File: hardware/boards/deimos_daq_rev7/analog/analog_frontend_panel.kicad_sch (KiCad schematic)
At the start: 18 parts, among them IC3001 BD42540FJ-CE2, IC3002 BD42540FJ-CE2, IC3003 BD42540FJ-CE2, J3001 Screw_Terminal_01x12, J3002 Screw_Terminal_01x10, J3003 Screw_Terminal_01x12, J3004 Screw_Terminal_01x12, J3005 Screw_Terminal_01x10, J3006 Screw_Terminal_01x12

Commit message: replace user power with gpio. wip to update frontend layout.
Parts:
- removed C3001, C3002: 0.1uF 50V 0603, Capacitor_SMD:C_0603_1608Metric, symbol Device:C_Small
- removed IC3001, IC3003: BD42540FJ-CE2, aaa:SOIC127P600X175-8N, symbol aaa:BD42540FJ-CE2
- removed J3001, J3003, J3004, J3006: Screw_Terminal_01x12, aaa:KF141V-2.54-12P, symbol Connector:Screw_Terminal_01x12
- removed J3002, J3005: Screw_Terminal_01x10, aaa:KF141V-2.54-10P, symbol Connector:Screw_Terminal_01x10
- added J1001, J1002, J1003, J1004, J1005, J1007: WJ15EDGRM-3.81-12P, aaa:WJ15EDGRM-3.81-12P, symbol aaa:WJ15EDGRM-3.81-12P
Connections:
- net 4-20mA Frontend/+24_EXC: now also J1004.11
- net 4-20mA Frontend/SIGNAL: now also J1004.12
- net 4-20mA Frontend1/+24_EXC: now also J1004.8
- net 4-20mA Frontend1/SIGNAL: now also J1004.9
- net 4-20mA Frontend2/+24_EXC: now also J1004.5
- net 4-20mA Frontend2/SIGNAL: now also J1004.6
- net 4-20mA Frontend3/+24_EXC: now also J1004.2
- net 4-20mA Frontend3/SIGNAL: now also J1004.3
- net GND: now also J1001.1, J1001.3, J1001.5, J1001.7, J1001.9, J1002.1, J1002.11, J1002.3, J1002.5, J1002.7, J1002.9, J1003.1, J1003.11, J1003.3, J1003.5, J1003.7, J1003.9, J1004.1, J1004.10, J1004.4, J1004.7, J1007.1, J1007.11, J1007.3, J1007.5, J1007.7, J1007.9
- net RTD Amp/R+: now also J1005.9
- net RTD Amp/R-: now also J1005.8
- net RTD Amp/W-: now also J1005.7
- net RTD Amp1/R+: now also J1005.6
- net RTD Amp1/R-: now also J1005.5
- net RTD Amp1/W-: now also J1005.4
- net RTD Amp2/R+: now also J1005.3
- net RTD Amp2/R-: now also J1005.2
- net RTD Amp2/W-: now also J1005.1
- net ain_0-15V_/VIN: now also J1003.8
- net ain_0-15V_1/VIN: now also J1003.6
- net ain_g1_/VIN: now also J1003.12
- net ain_g1_1/VIN: now also J1003.10
- net ain_g25p7_/VIN: now also J1003.4
- net ain_g666p333_/VIN: now also J1003.2
- net dac_buf/VOUT: now also J1002.2
- net dac_buf1/VOUT: now also J1002.4
- net pwm_in_buf/VIN: now also J1001.4
- net pwm_in_buf1/VIN: now also J1001.2
- net pwm_in_buf2/VIN: now also J1001.10
- net pwm_in_buf3/VIN: now also J1001.8
- net pwm_in_buf4/VIN: now also J1001.6
- net pwm_out_buf/VOUT: now also J1002.6
- net pwm_out_buf1/VOUT: now also J1002.8
- net pwm_out_buf2/VOUT: now also J1002.10
- net pwm_out_buf3/VOUT: now also J1002.12
- new net pwm_in_buf5/VIN: J1007.2
- new net pwm_in_buf6/VIN: J1007.4
- new net pwm_in_buf7/VIN: J1007.6
- new net pwm_out_buf4/VOUT: J1007.8
- new net pwm_out_buf5/VOUT: J1007.10
- new net pwm_out_buf6/VOUT: J1007.12
- no-connect marks 1 -> 5
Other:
- added sheet pwm_in_buf5 (pwm_in_buf.kicad_sch)
- added sheet pwm_in_buf6 (pwm_in_buf.kicad_sch)
- added sheet pwm_in_buf7 (pwm_in_buf.kicad_sch)
- added sheet pwm_out_buf4 (pwm_out_buf.kicad_sch)
- added sheet pwm_out_buf5 (pwm_out_buf.kicad_sch)
- added sheet pwm_out_buf6 (pwm_out_buf.kicad_sch)
- note added: "GPIO w/ OVP"
- note removed: "70mA total"
- note removed: "LDO for short-circuit protection"
- note removed: "User Power"

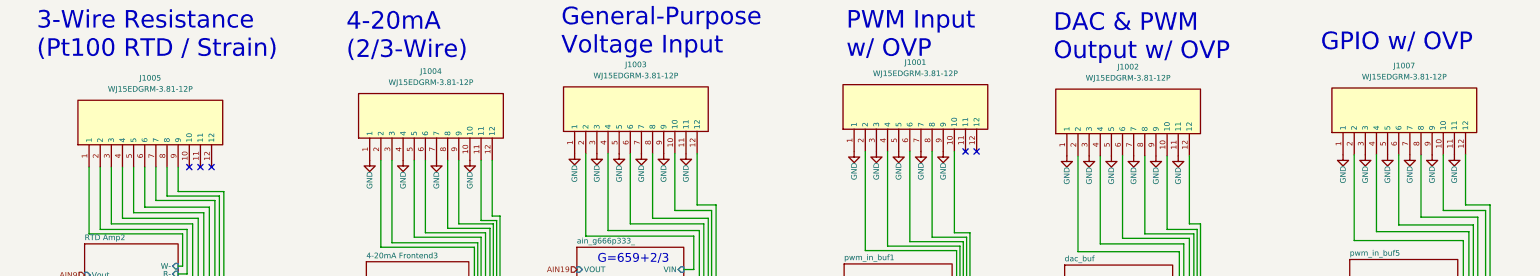
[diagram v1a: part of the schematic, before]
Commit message: flip pin order in symbol for pluggable terminal block
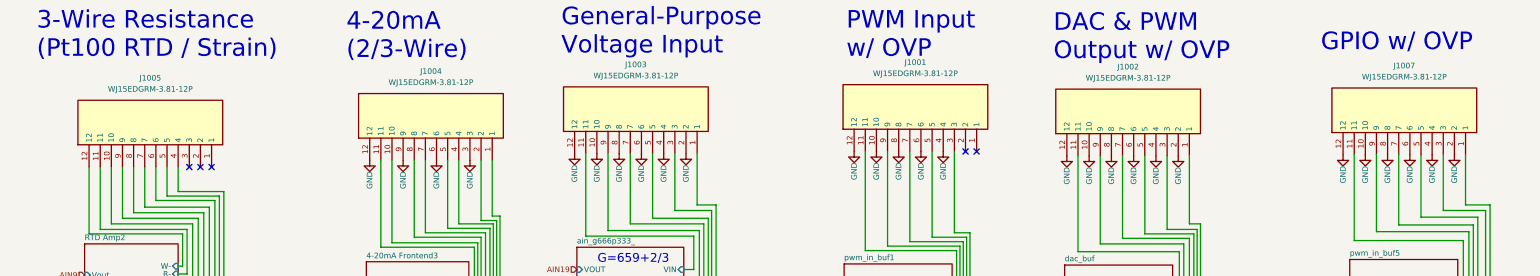
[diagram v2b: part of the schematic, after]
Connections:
- net 4-20mA Frontend/+24_EXC: now also J1004.2; no longer J1004.11
- net 4-20mA Frontend/SIGNAL: now also J1004.1; no longer J1004.12
- net 4-20mA Frontend1/+24_EXC: now also J1004.5; no longer J1004.8
- net 4-20mA Frontend1/SIGNAL: now also J1004.4; no longer J1004.9
- net 4-20mA Frontend2/+24_EXC: now also J1004.8; no longer J1004.5
- net 4-20mA Frontend2/SIGNAL: now also J1004.7; no longer J1004.6
- net 4-20mA Frontend3/+24_EXC: now also J1004.11; no longer J1004.2
- net 4-20mA Frontend3/SIGNAL: now also J1004.10; no longer J1004.3
- net GND: now also J1001.10, J1001.12, J1001.4, J1001.6, J1001.8, J1002.10, J1002.12, J1002.2, J1002.4, J1002.6, J1002.8, J1003.10, J1003.12, J1003.2, J1003.4, J1003.6, J1003.8, J1004.12, J1004.3, J1004.6, J1004.9, J1007.10, J1007.12, J1007.2, J1007.4, J1007.6, J1007.8; no longer J1001.1, J1001.3, J1001.5, J1001.7, J1001.9, J1002.1, J1002.11, J1002.3, J1002.5, J1002.7, J1002.9, J1003.1, J1003.11, J1003.3, J1003.5, J1003.7, J1003.9, J1004.1, J1004.10, J1004.4, J1004.7, J1007.1, J1007.11, J1007.3, J1007.5, J1007.7, J1007.9
- net RTD Amp/R+: now also J1005.4; no longer J1005.9
- net RTD Amp/R-: now also J1005.5; no longer J1005.8
- net RTD Amp/W-: now also J1005.6; no longer J1005.7
- net RTD Amp1/R+: now also J1005.7; no longer J1005.6
- net RTD Amp1/R-: now also J1005.8; no longer J1005.5
- net RTD Amp1/W-: now also J1005.9; no longer J1005.4
- net RTD Amp2/R+: now also J1005.10; no longer J1005.3
- net RTD Amp2/R-: now also J1005.11; no longer J1005.2
- net RTD Amp2/W-: now also J1005.12; no longer J1005.1
- net ain_0-15V_/VIN: now also J1003.5; no longer J1003.8
- net ain_0-15V_1/VIN: now also J1003.7; no longer J1003.6
- net ain_g1_/VIN: now also J1003.1; no longer J1003.12
- net ain_g1_1/VIN: now also J1003.3; no longer J1003.10
- net ain_g25p7_/VIN: now also J1003.9; no longer J1003.4
- net ain_g666p333_/VIN: now also J1003.11; no longer J1003.2
- net dac_buf/VOUT: now also J1002.11; no longer J1002.2
- net dac_buf1/VOUT: now also J1002.9; no longer J1002.4
- net pwm_in_buf/VIN: now also J1001.9; no longer J1001.4
- net pwm_in_buf1/VIN: now also J1001.11; no longer J1001.2
- net pwm_in_buf2/VIN: now also J1001.3; no longer J1001.10
- net pwm_in_buf3/VIN: now also J1001.5; no longer J1001.8
- net pwm_in_buf4/VIN: now also J1001.7; no longer J1001.6
- net pwm_in_buf5/VIN: now also J1007.11; no longer J1007.2
- net pwm_in_buf6/VIN: now also J1007.9; no longer J1007.4
- net pwm_in_buf7/VIN: now also J1007.7; no longer J1007.6
- net pwm_out_buf/VOUT: now also J1002.7; no longer J1002.6
- net pwm_out_buf1/VOUT: now also J1002.5; no longer J1002.8
- net pwm_out_buf2/VOUT: now also J1002.3; no longer J1002.10
- net pwm_out_buf3/VOUT: now also J1002.1; no longer J1002.12
- net pwm_out_buf4/VOUT: now also J1007.5; no longer J1007.8
- net pwm_out_buf5/VOUT: now also J1007.3; no longer J1007.10
- net pwm_out_buf6/VOUT: now also J1007.1; no longer J1007.12

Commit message: position connectors
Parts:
- renumbered J1005 to J3001, J1004 to J3002, J1003 to J3003, J1001 to J3004, J1002 to J3005, J1007 to J3006
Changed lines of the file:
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@@
 		(dnp no)
 		(fields_autoplaced yes)
-		(property "Reference" "J1005"
+		(property "Reference" "J3001"
 			(at 147.32 28.448 90)
 			(effects
@@
 		)
 		(instances
+			(project "analog_i"
+				(path "/5a60c4b1-b6cb-416e-8883-8291fa089b87/c2baf18d-2b19-4edb-98b3-535275ee271f"
+					(reference "J3001")
+					(unit 1)
+				)
+			)
 			(project "analog_frontend_panel"
 				(path "/c241d083-1323-4b4a-a540-956d0afb7b72"
@@
 		(dnp no)
 		(fields_autoplaced yes)
-		(property "Reference" "J1007"
+		(property "Reference" "J3006"
 			(at 433.324 25.654 90)
 			(effects
@@
 		)
 		(instances
+			(project "analog_i"
+				(path "/5a60c4b1-b6cb-416e-8883-8291fa089b87/c2baf18d-2b19-4edb-98b3-535275ee271f"
+					(reference "J3006")
+					(unit 1)
+				)
+			)
 			(project "analog_frontend_panel"
 				(path "/c241d083-1323-4b4a-a540-956d0afb7b72"
@@
 		(dnp no)
 		(fields_autoplaced yes)
-		(property "Reference" "J1003"
+		(property "Reference" "J3003"
 			(at 258.064 25.4 90)
 			(effects
@@
 		)
 		(instances
+			(project "analog_i"
+				(path "/5a60c4b1-b6cb-416e-8883-8291fa089b87/c2baf18d-2b19-4edb-98b3-535275ee271f"
+					(reference "J3003")
+					(unit 1)
+				)
+			)
 			(project "analog_frontend_panel"
 				(path "/c241d083-1323-4b4a-a540-956d0afb7b72"
@@
 		(dnp no)
 		(fields_autoplaced yes)
-		(property "Reference" "J1004"
+		(property "Reference" "J3002"
 			(at 211.328 26.924 90)
 			(effects
@@
 		)
 		(instances
+			(project "analog_i"
+				(path "/5a60c4b1-b6cb-416e-8883-8291fa089b87/c2baf18d-2b19-4edb-98b3-535275ee271f"
+					(reference "J3002")
+					(unit 1)
+				)
+			)
 			(project "analog_frontend_panel"
 				(path "/c241d083-1323-4b4a-a540-956d0afb7b72"
@@
 		(on_board yes)
 		(dnp no)
-		(property "Reference" "#PWR1028"
+		(property "Reference" "#PWR106"
 			(at 429.514 52.324 0)
 			(effects
@@
 		)
 		(instances
+			(project "analog_i"
+				(path "/5a60c4b1-b6cb-416e-8883-8291fa089b87/c2baf18d-2b19-4edb-98b3-535275ee271f"
+					(reference "#PWR106")
+					(unit 1)
+				)
+			)
 			(project "analog_frontend_panel"
 				(path "/c241d083-1323-4b4a-a540-956d0afb7b72"
@@
 		(dnp no)
 		(fields_autoplaced yes)
-		(property "Reference" "J1001"
+		(property "Reference" "J3004"
 			(at 321.818 24.892 90)
 			(effects
@@
 		)
 		(instances
+			(project "analog_i"
+				(path "/5a60c4b1-b6cb-416e-8883-8291fa089b87/c2baf18d-2b19-4edb-98b3-535275ee271f"
+					(reference "J3004")
+					(unit 1)
+				)
+			)
 			(project "analog_frontend_panel"
 				(path "/c241d083-1323-4b4a-a540-956d0afb7b72"
@@
 		(dnp no)
 		(fields_autoplaced yes)
-		(property "Reference" "J1002"
+		(property "Reference" "J3005"
 			(at 370.332 25.908 90)
 			(effects
@@
 		)
 		(instances
+			(project "analog_i"
+				(path "/5a60c4b1-b6cb-416e-8883-8291fa089b87/c2baf18d-2b19-4edb-98b3-535275ee271f"
+					(reference "J3005")
+					(unit 1)
+				)
+			)
 			(project ""
 				(path "/c241d083-1323-4b4a-a540-956d0afb7b72"
@@
 		(on_board yes)
 		(dnp no)
-		(property "Reference" "#PWR1029"
+		(property "Reference" "#PWR110"
 			(at 434.594 52.324 0)
 			(effects
@@
 		)
 		(instances
+			(project "analog_i"
+				(path "/5a60c4b1-b6cb-416e-8883-8291fa089b87/c2baf18d-2b19-4edb-98b3-535275ee271f"
+					(reference "#PWR110")
+					(unit 1)
+				)
+			)
 			(project "analog_frontend_panel"
 				(path "/c241d083-1323-4b4a-a540-956d0afb7b72"
@@
 		(on_board yes)
 		(dnp no)
-		(property "Reference" "#PWR1027"
+		(property "Reference" "#PWR109"
 			(at 424.434 52.324 0)
 			(effects
@@
 		)
 		(instances
+			(project "analog_i"
+				(path "/5a60c4b1-b6cb-416e-8883-8291fa089b87/c2baf18d-2b19-4edb-98b3-535275ee271f"
+					(reference "#PWR109")
+					(unit 1)
+				)
+			)
 			(project "analog_frontend_panel"
 				(path "/c241d083-1323-4b4a-a540-956d0afb7b72"
@@
 		(on_board yes)
 		(dnp no)
-		(property "Reference" "#PWR1032"
+		(property "Reference" "#PWR104"
 			(at 444.754 52.324 0)
 			(effects
@@
 		)
 		(instances
+			(project "analog_i"
+				(path "/5a60c4b1-b6cb-416e-8883-8291fa089b87/c2baf18d-2b19-4edb-98b3-535275ee271f"
+					(reference "#PWR104")
+					(unit 1)
+				)
+			)
 			(project "analog_frontend_panel"
 				(path "/c241d083-1323-4b4a-a540-956d0afb7b72"
@@
 		(on_board yes)
 		(dnp no)
-		(property "Reference" "#PWR1031"
+		(property "Reference" "#PWR105"
 			(at 439.674 52.324 0)
 			(effects
@@
 		)
 		(instances
+			(project "analog_i"
+				(path "/5a60c4b1-b6cb-416e-8883-8291fa089b87/c2baf18d-2b19-4edb-98b3-535275ee271f"
+					(reference "#PWR105")
+					(unit 1)
+				)
+			)
 			(project "analog_frontend_panel"
 				(path "/c241d083-1323-4b4a-a540-956d0afb7b72"
@@
 		(on_board yes)
 		(dnp no)
-		(property "Reference" "#PWR1026"
+		(property "Reference" "#PWR111"
 			(at 419.354 52.324 0)
 			(effects
@@
 		)
 		(instances
+			(project "analog_i"
+				(path "/5a60c4b1-b6cb-416e-8883-8291fa089b87/c2baf18d-2b19-4edb-98b3-535275ee271f"
+					(reference "#PWR111")
+					(unit 1)
+				)
+			)
 			(project "analog_frontend_panel"
 				(path "/c241d083-1323-4b4a-a540-956d0afb7b72"

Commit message: wip to update layout for frontend
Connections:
- net pwm_in_buf5/VIN is gone; now on net pwm_in_buf6/VIN: J3006.11
- net pwm_in_buf6/VIN: no longer J3006.9
- net pwm_in_buf7/VIN: now also J3006.9; no longer J3006.7
- net pwm_out_buf4/VOUT: now also J3006.7; no longer J3006.5
- net pwm_out_buf5/VOUT: now also J3006.5; no longer J3006.3
- net pwm_out_buf6/VOUT: now also J3006.3; no longer J3006.1
- new net pwm_out_buf7/VOUT: J3006.1
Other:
- removed sheet pwm_in_buf5
- added sheet pwm_out_buf7 (pwm_out_buf.kicad_sch)

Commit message: first pass adding dsub breakout schematic, routing, and labels
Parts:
- added J3007: XG4C-2631, aaa:SHDR26W70P254_2X13_4030X820X900P, symbol aaa:XG4C-2631
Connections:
- net GND: now also J3007.1, J3007.11, J3007.13, J3007.15, J3007.17, J3007.19, J3007.21, J3007.23, J3007.25, J3007.3, J3007.5, J3007.7, J3007.9
- net ain_0-15V_/VIN renamed 15V_0
- net 15V_0: now also J3007.22
- net ain_0-15V_1/VIN renamed 15V_1
- net 15V_1: now also J3007.24
- net ain_g1_/VIN renamed 2p5V_0
- net 2p5V_0: now also J3007.18
- net ain_g1_1/VIN renamed 2p5V_1
- net 2p5V_1: now also J3007.20
- net ain_g25p7_/VIN renamed 25p7x
- net 25p7x: now also J3007.26
- net ain_g666p333_/VIN renamed 660x
- net dac_buf/VOUT renamed DAC0
- net DAC0: now also J3007.2
- net dac_buf1/VOUT renamed DAC1
- net DAC1: now also J3007.4
- net pwm_in_buf6/VIN renamed DI0
- net DI0: now also J3007.6
- net pwm_in_buf7/VIN renamed DI1
- net DI1: now also J3007.8
- net pwm_out_buf4/VOUT renamed DO0
- net DO0: now also J3007.10
- net pwm_out_buf5/VOUT renamed DO1
- net DO1: now also J3007.12
- net pwm_out_buf6/VOUT renamed DO2
- net DO2: now also J3007.14
- net pwm_out_buf7/VOUT renamed DO3
- net DO3: now also J3007.16
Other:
- note added: "IDC/DSUB Breakout"

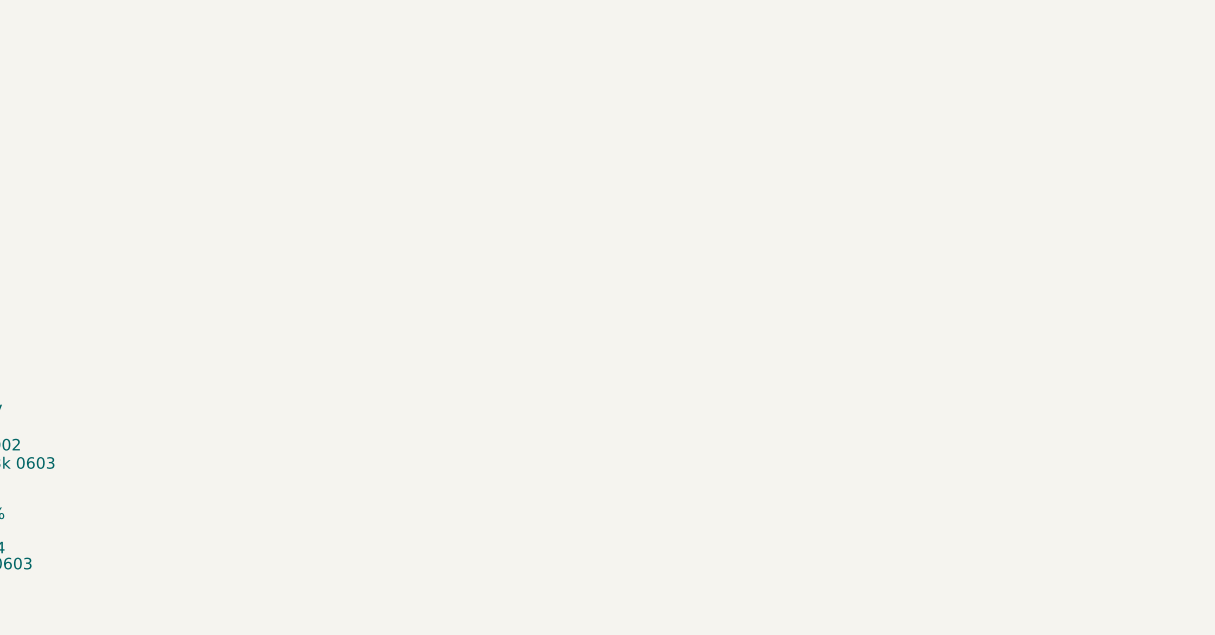
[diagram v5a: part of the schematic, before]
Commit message: update schematic with regulated OVP rail
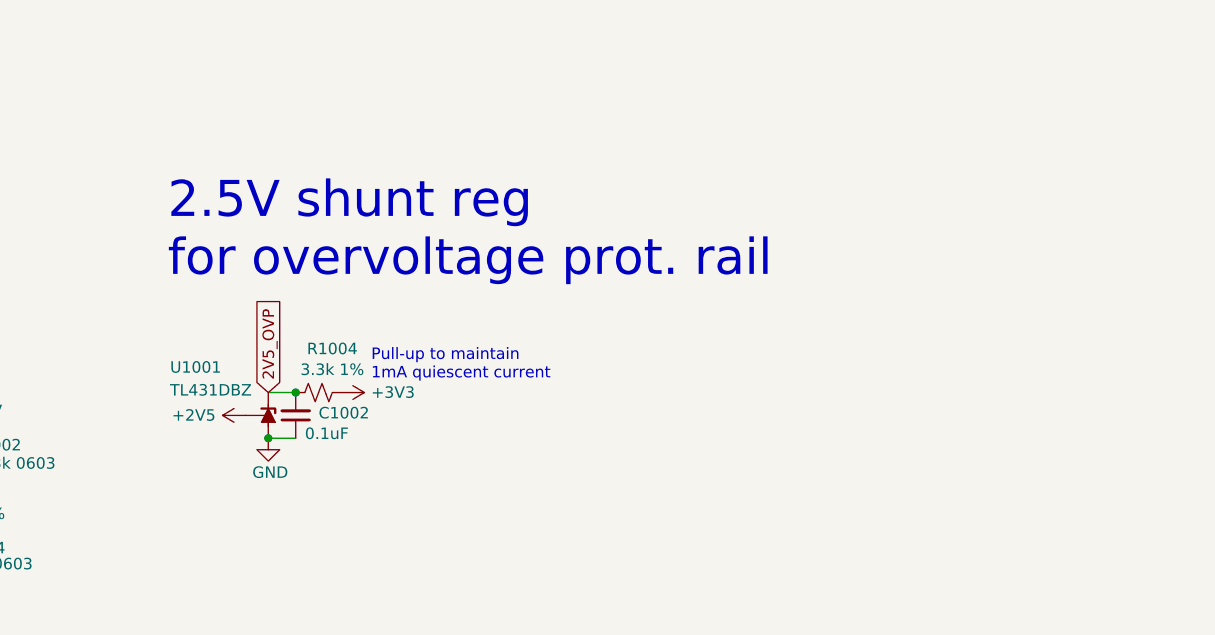
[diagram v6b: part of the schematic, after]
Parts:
- added C1002: 0.1uF, Capacitor_SMD:C_0402_1005Metric, symbol Device:C_Small
- added R1004: 3.3k 1%, Resistor_SMD:R_0402_1005Metric, symbol Device:R_Small_US
- added U1001: TL431DBZ, Package_TO_SOT_SMD:SOT-23, symbol Reference_Voltage:TL431DBZ
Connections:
- net GND: now also C1002.1, U1001.3 (A)
- new net +2V5: U1001.2 (REF)
- new net +3V3: R1004.2
- new net 2V5_OVP: C1002.2, R1004.1, U1001.1 (K)
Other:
- note added: "2.5V shunt reg for overvoltage prot. rail"
- note added: "Pull-up to maintain 1mA quiescent current"

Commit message: set LCSC PNs for new connectors. wip to update layout for changes to ovp and dac
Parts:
- J3001, J3002, J3003, J3004, J3005, J3006: LCSC (none) -> C508940
- J3007: LCSC (none) -> C397108
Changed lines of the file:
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@@
 			)
 		)
+		(property "LCSC" "C508940"
+			(at 133.35 48.768 0)
+			(effects
+				(font
+					(size 1.27 1.27)
+				)
+				(hide yes)
+			)
+		)
 		(pin "8"
 		)
@@
 			)
 		)
+		(property "LCSC" "C508940"
+			(at 419.354 45.974 0)
+			(effects
+				(font
+					(size 1.27 1.27)
+				)
+				(hide yes)
+			)
+		)
 		(pin "8"
 		)
@@
 			)
 		)
+		(property "LCSC" "C508940"
+			(at 244.094 45.72 0)
+			(effects
+				(font
+					(size 1.27 1.27)
+				)
+				(hide yes)
+			)
+		)
 		(pin "8"
 		)
@@
 			)
 		)
+		(property "LCSC" "C508940"
+			(at 197.358 47.244 0)
+			(effects
+				(font
+					(size 1.27 1.27)
+				)
+				(hide yes)
+			)
+		)
 		(pin "8"
 		)
@@
 			)
 		)
+		(property "LCSC" "C508940"
+			(at 307.848 45.212 0)
+			(effects
+				(font
+					(size 1.27 1.27)
+				)
+				(hide yes)
+			)
+		)
 		(pin "8"
 		)
@@
 			)
 		)
+		(property "LCSC" "C508940"
+			(at 356.362 46.228 0)
+			(effects
+				(font
+					(size 1.27 1.27)
+				)
+				(hide yes)
+			)
+		)
 		(pin "8"
 		)
@@
 				(hide yes)
 			)
+		)
+		(property "LCSC" "C397108"
+			(at 524.002 64.262 0)
+			(effects
+				(font
+					(size 1.27 1.27)
+				)
+				(hide yes)
+			)

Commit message: wip to export more gpio pins
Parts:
- renumbered C1002 to C3001, R1004 to R3005, U1001 to U3001
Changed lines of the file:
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@@
 		(on_board yes)
 		(dnp no)
-		(property "Reference" "#PWR1005"
+		(property "Reference" "#PWR180"
 			(at 186.944 261.112 0)
 			(effects
@@
 		)
 		(instances
+			(project "analog_i"
+				(path "/5a60c4b1-b6cb-416e-8883-8291fa089b87/c2baf18d-2b19-4edb-98b3-535275ee271f"
+					(reference "#PWR180")
+					(unit 1)
+				)
+			)
 			(project "analog_frontend_panel"
 				(path "/c241d083-1323-4b4a-a540-956d0afb7b72"
@@
 		(on_board yes)
 		(dnp no)
-		(property "Reference" "C1002"
+		(property "Reference" "C3001"
 			(at 191.262 260.858 0)
 			(effects
@@
 		)
 		(instances
+			(project "analog_i"
+				(path "/5a60c4b1-b6cb-416e-8883-8291fa089b87/c2baf18d-2b19-4edb-98b3-535275ee271f"
+					(reference "C3001")
+					(unit 1)
+				)
+			)
 			(project "analog_frontend_panel"
 				(path "/c241d083-1323-4b4a-a540-956d0afb7b72"
@@
 		(on_board yes)
 		(dnp no)
-		(property "Reference" "R1004"
+		(property "Reference" "R3005"
 			(at 192.786 253.7206 90)
 			(effects
@@
 		)
 		(instances
+			(project "analog_i"
+				(path "/5a60c4b1-b6cb-416e-8883-8291fa089b87/c2baf18d-2b19-4edb-98b3-535275ee271f"
+					(reference "R3005")
+					(unit 1)
+				)
+			)
 			(project "analog_frontend_panel"
 				(path "/c241d083-1323-4b4a-a540-956d0afb7b72"
@@
 		(on_board yes)
 		(dnp no)
-		(property "Reference" "U1001"
+		(property "Reference" "U3001"
 			(at 174.752 255.778 90)
 			(effects
@@
 		)
 		(instances
+			(project "analog_i"
+				(path "/5a60c4b1-b6cb-416e-8883-8291fa089b87/c2baf18d-2b19-4edb-98b3-535275ee271f"
+					(reference "U3001")
+					(unit 1)
+				)
+			)
 			(project ""
 				(path "/c241d083-1323-4b4a-a540-956d0afb7b72"
@@
 		(dnp no)
 		(fields_autoplaced yes)
-		(property "Reference" "#PWR1007"
+		(property "Reference" "#PWR207"
 			(at 189.992 258.572 0)
 			(effects
@@
 		)
 		(instances
+			(project "analog_i"
+				(path "/5a60c4b1-b6cb-416e-8883-8291fa089b87/c2baf18d-2b19-4edb-98b3-535275ee271f"
+					(reference "#PWR207")
+					(unit 1)
+				)
+			)
 			(project "analog_frontend_panel"
 				(path "/c241d083-1323-4b4a-a540-956d0afb7b72"
@@
 		(on_board yes)
 		(dnp no)
-		(property "Reference" "#PWR1003"
+		(property "Reference" "#PWR196"
 			(at 185.674 270.002 0)
 			(effects
@@
 		)
 		(instances
+			(project "analog_i"
+				(path "/5a60c4b1-b6cb-416e-8883-8291fa089b87/c2baf18d-2b19-4edb-98b3-535275ee271f"
+					(reference "#PWR196")
+					(unit 1)
+				)
+			)
 			(project "analog_frontend_panel"
 				(path "/c241d083-1323-4b4a-a540-956d0afb7b72"
